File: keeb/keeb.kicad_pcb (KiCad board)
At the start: 2 copper layers, 138 parts, among them J1 USB_A, J2 USB_A, J3 USB_A, J4 USB_A, P1 USB_C_Plug_USB2.0, P2 USB_C_Plug_USB2.0, SW1 SW_Push, SW10 SW_Push, SW11 SW_Push, SW12 SW_Push, SW13 SW_Push, SW14 SW_Push, SW15 SW_Push, SW16 SW_Push, SW17 SW_Push, SW18 SW_Push, SW19 SW_Push, SW2 SW_Push, SW20 SW_Push, SW21 SW_Push, SW22 SW_Push, SW23 SW_Push, SW24 SW_Push, SW25 SW_Push, SW26 SW_Push, SW27 SW_Push, SW28 SW_Push, SW29 SW_Push, SW3 SW_Push, SW30 SW_Push, SW31 SW_Push, SW32 SW_Push, SW33 SW_Push, SW34 SW_Push, SW35 SW_Push, SW36 SW_Push, SW37 SW_Push, SW38 SW_Push, SW39 SW_Push, SW4 SW_Push, SW40 SW_Push, SW41 SW_Push, SW42 SW_Push, SW43 SW_Push, SW44 SW_Push, SW45 SW_Push, SW46 SW_Push, SW47 SW_Push, SW48 SW_Push, SW49 SW_Push, SW5 SW_Push, SW50 SW_Push, SW6 SW_Push, SW7 SW_Push, SW8 SW_Push, SW9 SW_Push, U1 XIAO-nRF52840-SMD, U2 XIAO-nRF52840-SMD, U3 USB2512-AEZG, U4 USB2512-AEZG

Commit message: worked on routing
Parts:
- removed H11, H13: MountingHole, keeb:mouse-bite-5mm-slot
- TP5, TP6: value HapticFeedbackMotor+ -> Motor+
- TP7, TP8: value HapticFeedbackMotor- -> Motor-
- moved TP5 133.3 mm to (146.7, 33.0)
- moved TP7 132.2 mm to (146.7, 40.6)
- moved J1 117.0 mm to (232.4, 34.3), turned to 180 degrees
- moved H8 116.2 mm to (39.4, 157.5)
- moved TP1 115.6 mm to (158.8, 57.1)
- moved TP3 112.7 mm to (167.6, 57.1)
- moved H9 102.7 mm to (139.1, 92.0), turned to 90 degrees
- moved J3 99.9 mm to (212.1, 34.3), turned to 180 degrees
- moved U1 99.4 mm to (162.6, 39.0)
- moved U4 99.4 mm to (57.1, 52.1)
- moved H4 98.3 mm to (43.2, 57.1)
- moved J2 96.7 mm to (47.9, 34.3), turned to 180 degrees
- moved J4 95.7 mm to (70.2, 34.3), turned to 180 degrees
- moved U2 93.7 mm to (118.1, 39.4)
- moved H7 92.5 mm to (144.8, 120.0)
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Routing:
- net row0: track 0.00 -> 527.5 mm, vias 0 -> 6
- net col3: track 0.00 -> 507.8 mm, vias 0 -> 3
- net col1: track 0.00 -> 487.3 mm, vias 0 -> 5
- net row1: track 0.00 -> 478.3 mm, vias 0 -> 11
- net row2: track 0.00 -> 464.0 mm, vias 0 -> 13
- net row3: track 0.00 -> 459.3 mm, vias 0 -> 13
- net col0: track 0.00 -> 454.1 mm, vias 0 -> 2
- net col2: track 0.00 -> 435.7 mm, vias 0 -> 6
- net row4: track 0.00 -> 391.6 mm, vias 0 -> 8
- net col4: track 0.00 -> 360.4 mm, vias 0 -> 5
- net GND: track 0.00 -> 341.8 mm, vias 0 -> 5
- net downVbus0: track 0.00 -> 310.5 mm, vias 0 -> 3
- net downVbus1: track 0.00 -> 260.3 mm
- net Net-(U3-VBUS_DET): track 0.00 -> 88.4 mm, vias 0 -> 2
- net data0: track 0.00 -> 70.9 mm, vias 0 -> 1
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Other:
- board outline added: 207 x 133.3 mm

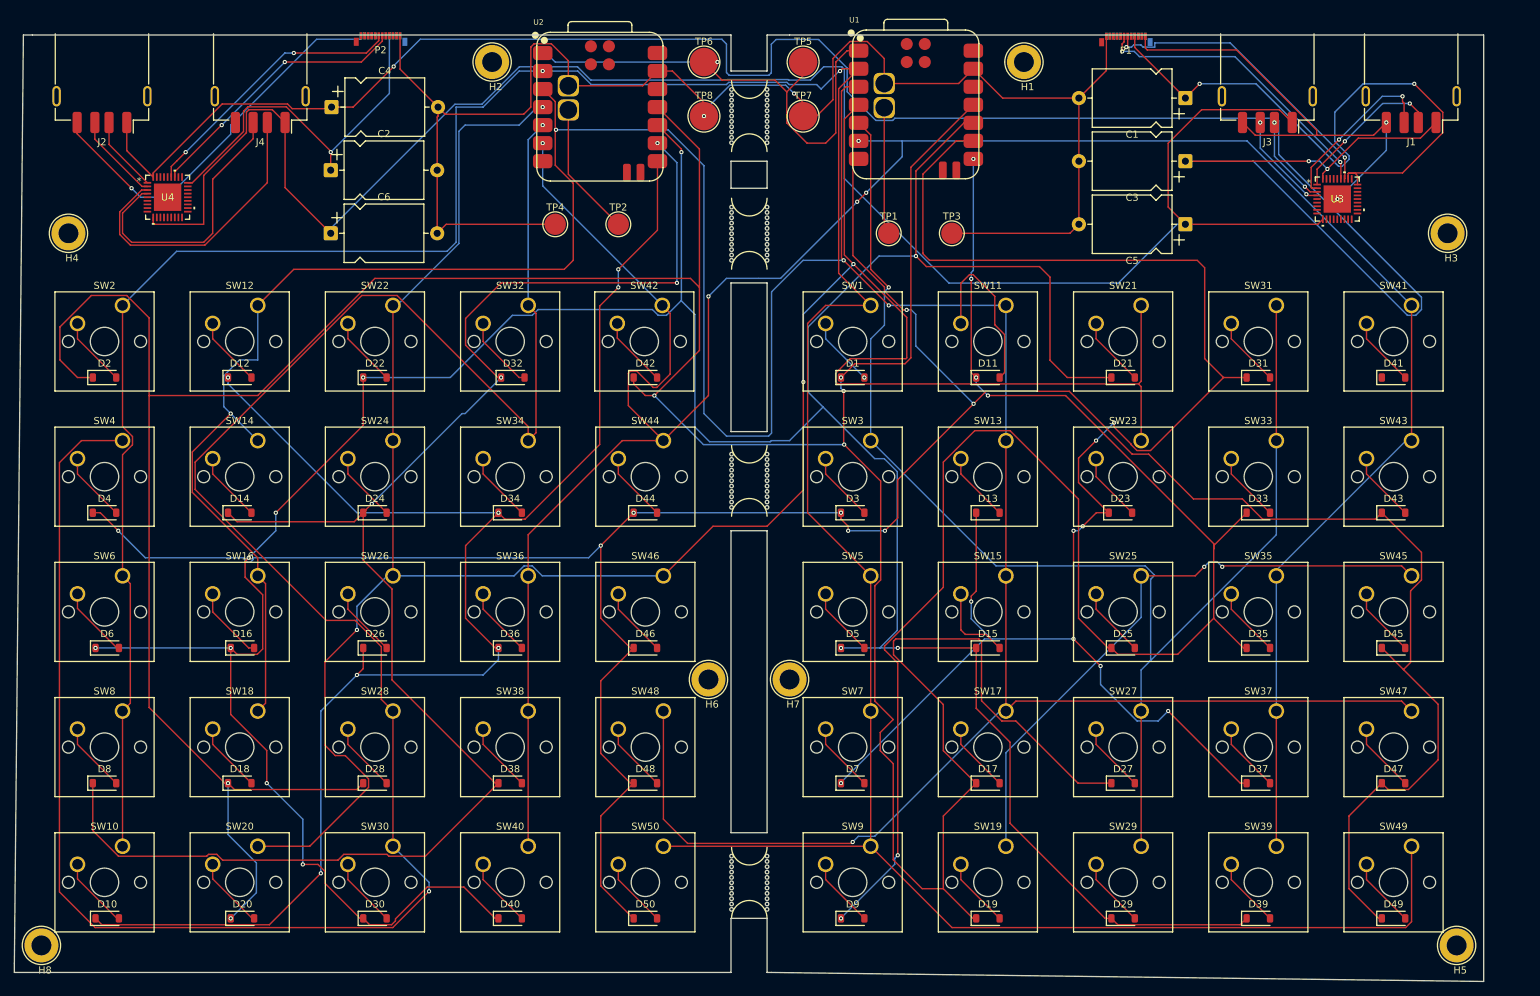
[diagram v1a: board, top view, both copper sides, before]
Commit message: finished routing, added the back Silkscreen, fixed DRC
I finished the leftover routing, added some images to the back silkscreen, and went through the DRC errors. There are still some problems with the USB-C port's clearance, but otherwise, the PCB is almost done. I'll try to get the Cad and FW done this week so I can wrap up and submit on Sat. PCB way says ~54$ for the pcb.
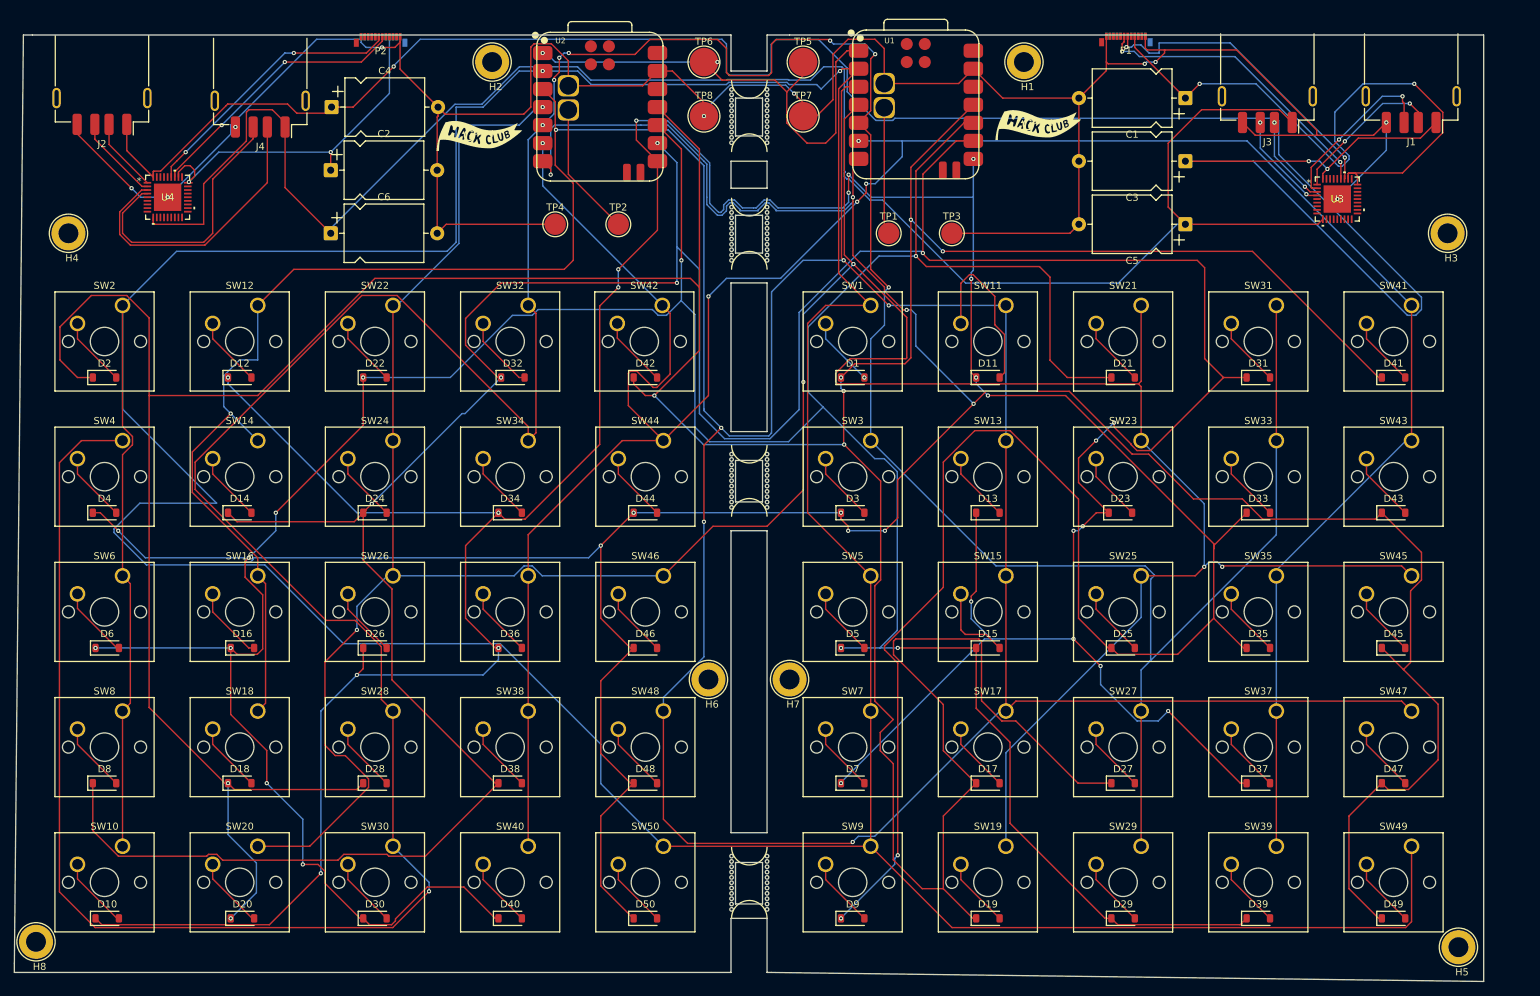
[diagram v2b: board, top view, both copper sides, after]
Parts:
- added G***: LOGO, LOGO, F.Cu at (179.8, 41.9)
- added G***: LOGO, LOGO, B.Cu at (214.7, 81.8)
- added G***: LOGO, LOGO, B.Cu at (107.4, 92.2)
- added G***: LOGO, LOGO, B.Cu at (52.7, 138.7)
- added G***: LOGO, LOGO, B.Cu at (52.2, 81.8)
- added G***: LOGO, LOGO, B.Cu at (220.3, 112.3)
- added G***: LOGO, LOGO, F.Cu at (101.1, 43.4)
- added G***: LOGO, LOGO, B.Cu at (71.5, 100.8)
- added G***: LOGO, LOGO, B.Cu at (157.8, 138.9)
- added G***: LOGO, LOGO, B.Cu at (109.6, 138.9)
- added G***: LOGO, LOGO, B.Cu at (165.6, 92.5)
- added G***: LOGO, LOGO, B.Cu at (215.0, 138.9)
- added G***: LOGO, LOGO, B.Cu at (196.2, 101.1)
- added G***: LOGO, LOGO, B.Cu at (81.8, 147.8)
- P1, P2: value USB_C_Plug_USB2.0 -> USB_C
- TP1, TP2: value TestPoint -> Batt+
- TP3, TP4: value TestPoint -> Batt-
- moved H8 0.92 mm to (38.6, 157.0)
- moved J4 0.63 mm to (70.2, 34.9)
- moved H5 0.36 mm to (239.0, 157.7)
- moved J2 0.26 mm to (47.9, 34.5)
- moved P2 0.13 mm to (87.2, 29.4)
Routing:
- net col0: track 454.1 -> 602.9 mm
- net row2: track 464.0 -> 540.8 mm, vias 13 -> 14
- net col3: track 507.8 -> 584.1 mm, vias 3 -> 8
- net row0: track 527.5 -> 603.1 mm, vias 6 -> 8
- net row3: track 459.3 -> 530.4 mm, vias 13 -> 16
- net row4: track 391.6 -> 455.8 mm, vias 8 -> 10
- net col1: track 487.3 -> 530.4 mm, vias 5 -> 7
- net col2: track 435.7 -> 457.1 mm
- net GND: track 341.8 -> 359.9 mm, vias 5 -> 10
- net Net-(P1-D-): track 42.5 -> 43.7 mm
- net Net-(U4-VBUS_DET): track 50.8 -> 50.0 mm, vias 1 -> 2
- net col4: track 360.4 -> 361.1 mm
- net downVbus0: track 310.5 -> 311.1 mm
- net data0: track 70.9 -> 71.4 mm, vias 1 -> 2
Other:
- outline, holes or cut-outs redrawn
- board text added: "Eshaan Ahuja 10/5/2025 Split Keyboard v1.0"
- board text added: "General info: split keyboard with built in USBC splitter into two USBA ports"

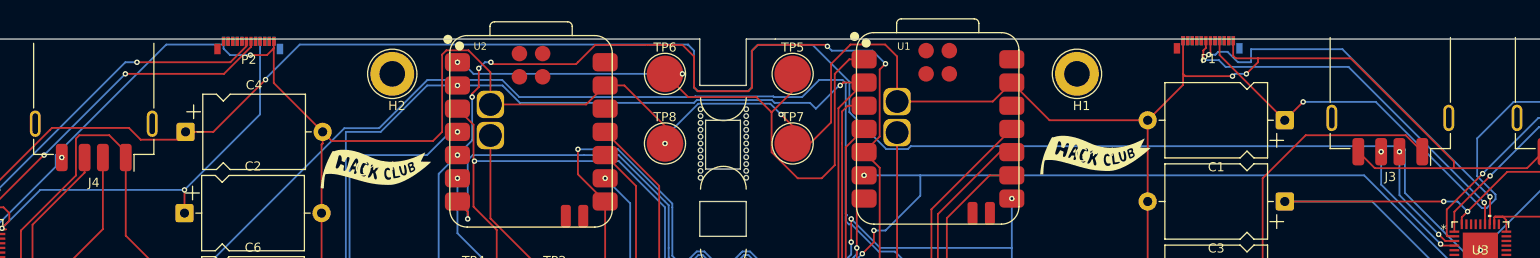
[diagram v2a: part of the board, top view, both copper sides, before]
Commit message: fixed some pcbway errors
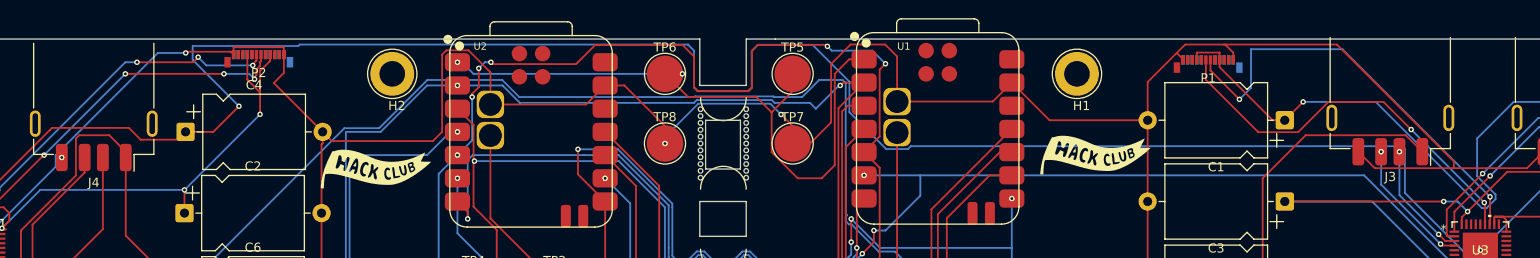
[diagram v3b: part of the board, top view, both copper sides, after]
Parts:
- moved P1 2.11 mm to (192.2, 31.5)
- moved P2 1.82 mm to (88.3, 30.9)
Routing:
- net downVbus0: track 311.1 -> 321.9 mm
- net Net-(U4-VBUS_DET): track 50.0 -> 54.0 mm, vias 2 -> 3
- net Net-(P1-D-): track 43.7 -> 47.5 mm
- net Net-(U3-VBUS_DET): track 88.4 -> 91.6 mm
- net Net-(P2-D-): track 37.9 -> 40.0 mm, vias 2 -> 4
- net Net-(P1-D+): track 41.4 -> 43.3 mm
- net Net-(P2-D+): track 38.3 -> 40.0 mm, vias 2 -> 4
- net GND: track 359.9 -> 359.1 mm, vias 10 -> 8

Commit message: readme
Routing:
- net col0: vias 2 -> 3
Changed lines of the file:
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@@
+	)
+	(segment
+		(start 50.8 82.042)
+		(end 50.8 84.378686)
+		(width 0.2)
+		(layer "F.Cu")
+		(net 89)
 	)
 	(segment
@@
 	(segment
 		(start 50.8 67.31)
-		(end 50.8 84.378686)
+		(end 50.8 82.042)
 		(width 0.2)
 		(layer "F.Cu")
@@
 		(net 89)
 	)
+	(via
+		(at 50.8 82.042)
+		(size 0.6)
+		(drill 0.3)
+		(layers "F.Cu" "B.Cu")
+		(net 89)
+	)
